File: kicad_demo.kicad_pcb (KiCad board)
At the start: 2 copper layers, 100 x 50 mm, 29 parts, among them P1 pwr, P2 key, Q1 BC546, Q2 BC546, Q3 BC546, Y1 7020 kHz

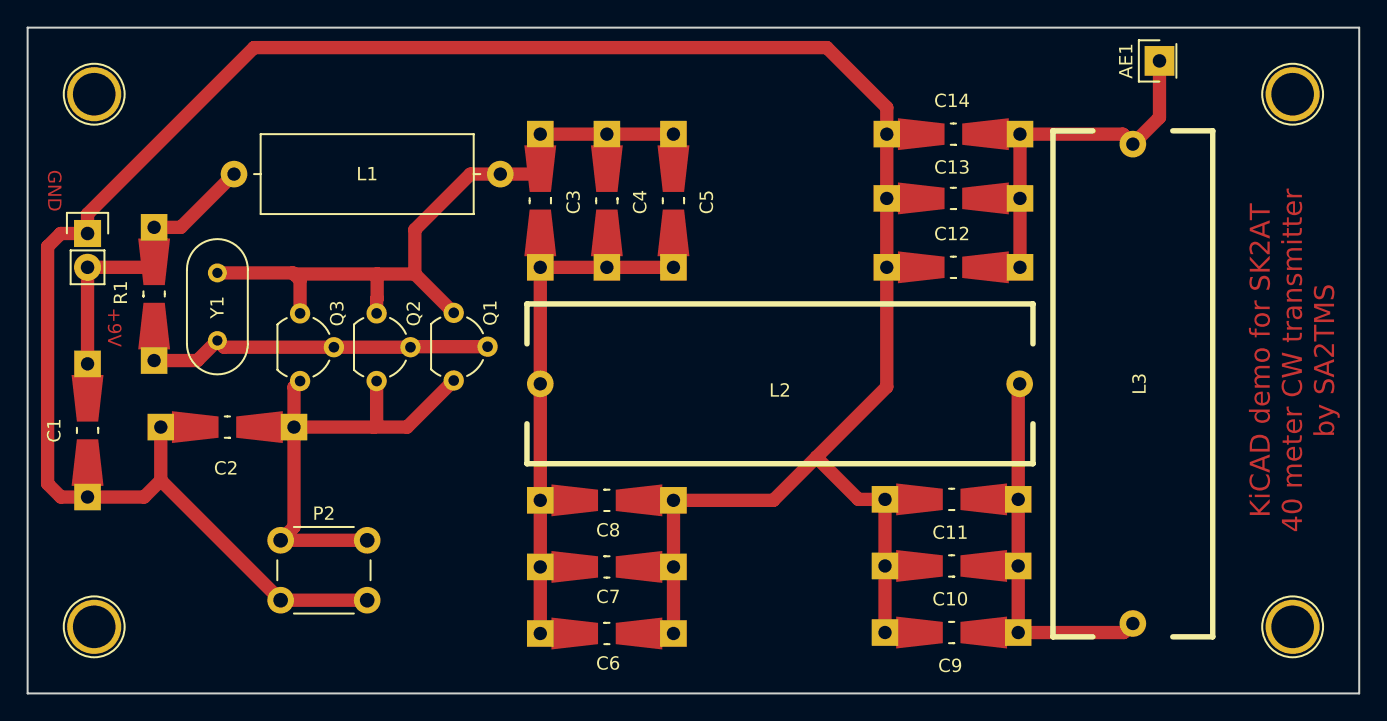
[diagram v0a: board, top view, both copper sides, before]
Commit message: Add test points, winding instruction on F.SilkS
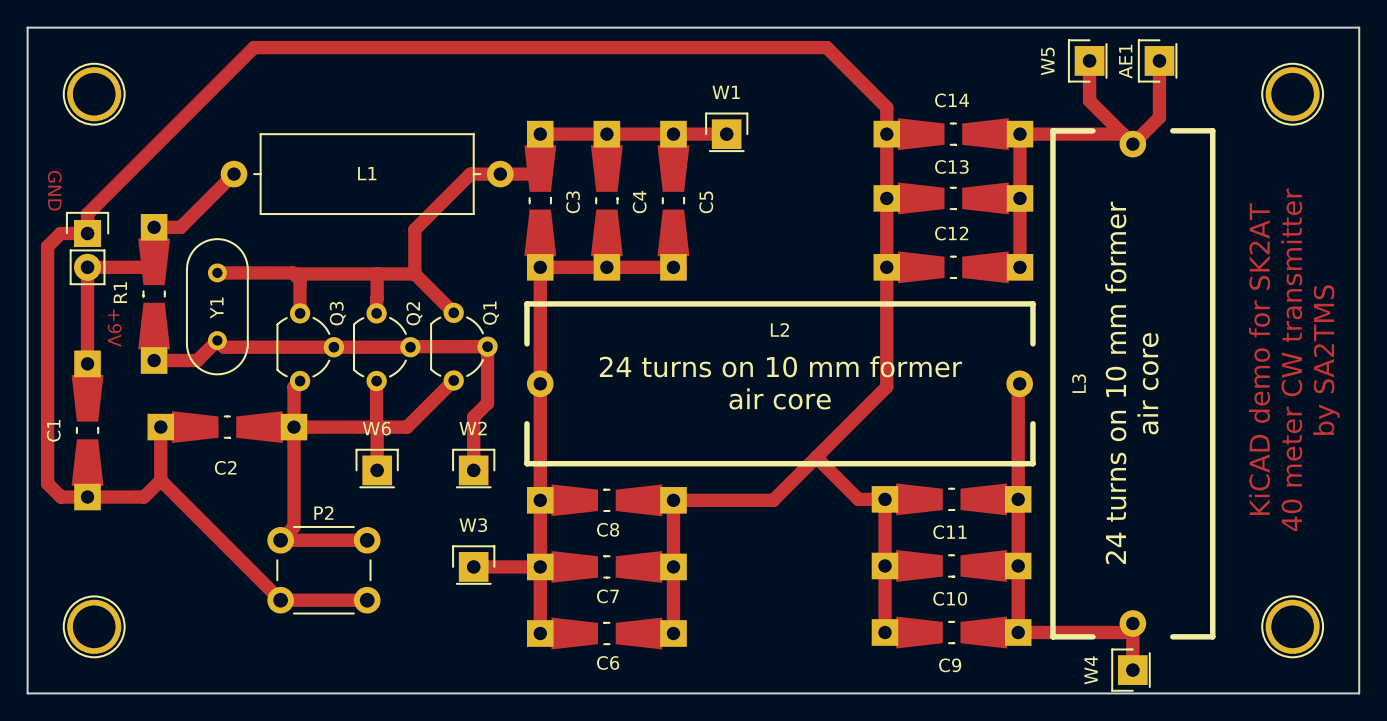
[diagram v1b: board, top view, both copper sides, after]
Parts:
- added W1: TEST_1P, Pin_Headers:Pin_Header_Straight_1x01, F.Cu at (102.5, 83.0)
- added W2: TEST_1P, Pin_Headers:Pin_Header_Straight_1x01, F.Cu at (83.5, 108.2)
- added W3: TEST_1P, Pin_Headers:Pin_Header_Straight_1x01, F.Cu at (83.5, 115.5)
- added W4: TEST_1P, Pin_Headers:Pin_Header_Straight_1x01, F.Cu at (133.0, 123.2)
- added W5: TEST_1P, Pin_Headers:Pin_Header_Straight_1x01, F.Cu at (129.8, 77.5)
- added W6: TEST_1P, Pin_Headers:Pin_Header_Straight_1x01, F.Cu at (76.2, 108.2)
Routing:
- net Net-(Q1-Pad2): track 28.5 -> 38.3 mm
- net Net-(AE1-Pad1): track 33.6 -> 41.2 mm
- net Net-(C3-Pad2): track 53.0 -> 58.0 mm
- net Net-(C3-Pad1): track 57.5 -> 61.5 mm
- net Net-(C10-Pad1): track 35.4 -> 38.9 mm
- net Net-(C2-Pad1): track 38.6 -> 42.1 mm
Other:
- board text added: "24 turns on 10 mm former air core"

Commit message: License under TAPR Open Hardware License Version 1.0
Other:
- board text added: "Licensed under the TAPR Open Hardware License Version 1.0"
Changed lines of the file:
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@@
     (links 82)
     (no_connects 0)
-    (area 49.924999 74.924999 150.075001 125.075001)
+    (area 49.02384 73.95238 150.100001 126.797619)
     (thickness 1.6)
-    (drawings 13)
+    (drawings 14)
     (tracks 126)
     (zones 0)
@@
   )
   (setup
-    (last_trace_width 1)
+    (last_trace_width 0.5)
     (user_trace_width 1)
     (user_trace_width 1.5)
@@
     )
   )
+  (gr_text "Licensed under the TAPR Open Hardware License Version 1.0" (at 103.75 72) (layer Cmts.User)
+    (effects (font (size 1.5 1.5) (thickness 0.3)))
+  )
   (gr_text "24 turns on 10 mm former\nair core" (at 133 101.75 90) (layer F.SilkS)

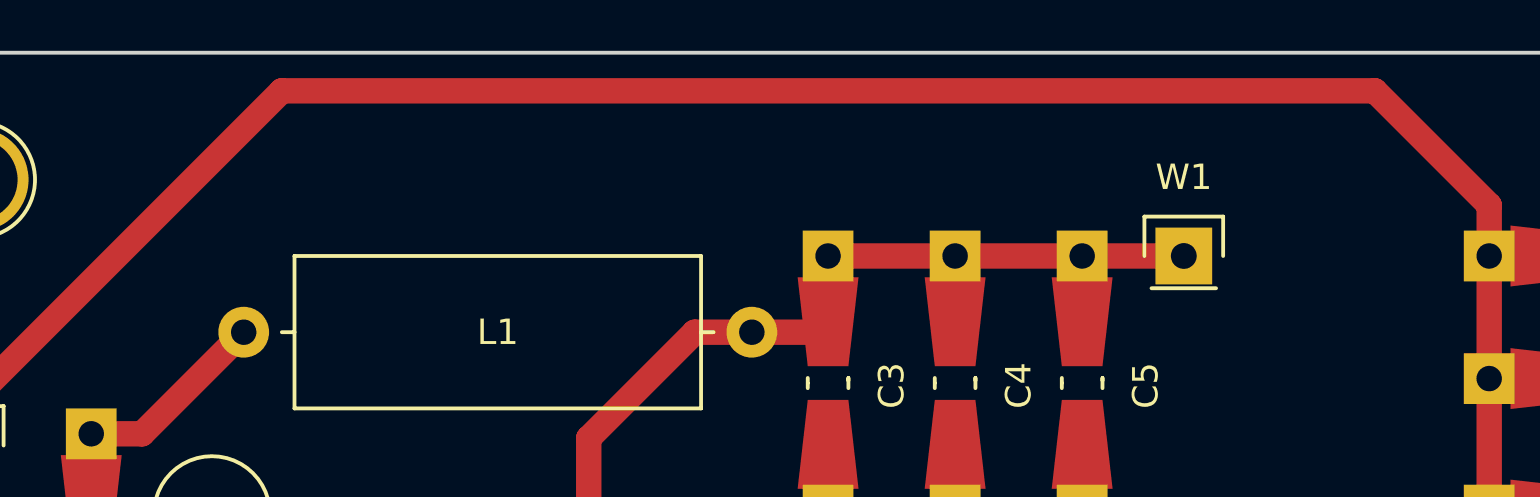
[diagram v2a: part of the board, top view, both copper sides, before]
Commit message: Add some useful power test points
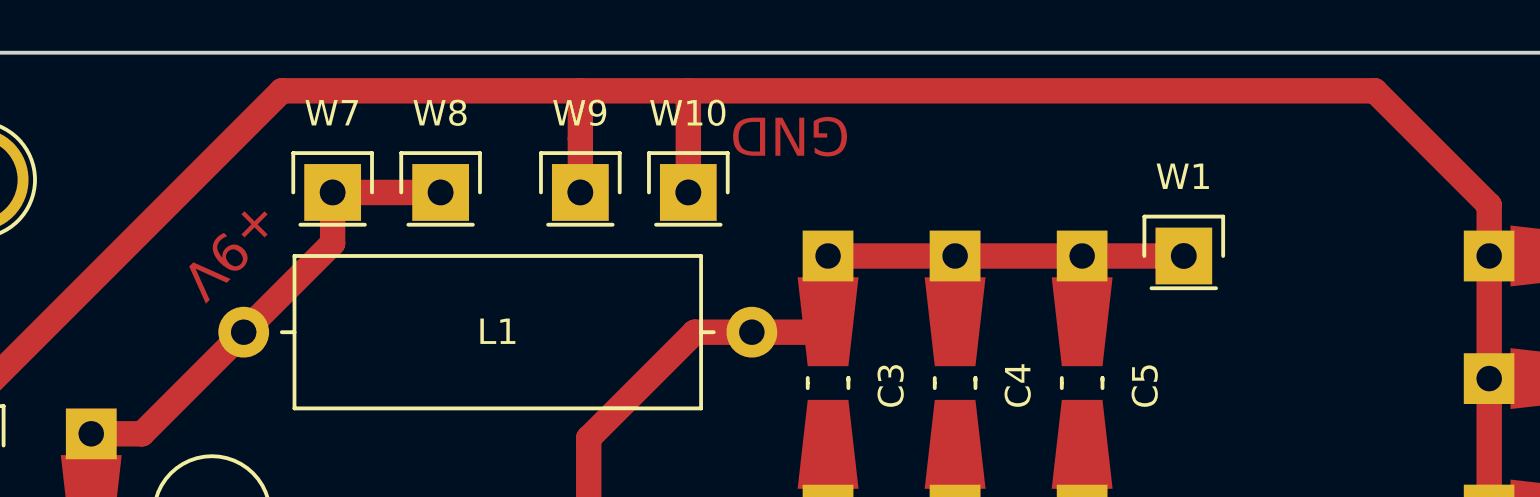
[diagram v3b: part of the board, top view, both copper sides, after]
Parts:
- added W10: TEST_1P, Pin_Headers:Pin_Header_Straight_1x01, F.Cu at (83.0, 80.5)
- added W7: TEST_1P, Pin_Headers:Pin_Header_Straight_1x01, F.Cu at (69.0, 80.5)
- added W8: TEST_1P, Pin_Headers:Pin_Header_Straight_1x01, F.Cu at (73.2, 80.5)
- added W9: TEST_1P, Pin_Headers:Pin_Header_Straight_1x01, F.Cu at (78.8, 80.5)
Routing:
- net +9V: track 25.3 -> 36.5 mm
- net GND: track 217.9 -> 225.9 mm
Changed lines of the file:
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@@
 (kicad_pcb (version 4) (host pcbnew 4.0.5+dfsg1-4)
   (general
-    (links 82)
-    (no_connects 0)
-    (area 49.02384 73.95238 150.100001 126.797619)
+    (links 86)
+    (no_connects 2)
+    (area 49.924999 74.924999 150.075001 125.075001)
     (thickness 1.6)
-    (drawings 14)
-    (tracks 126)
+    (drawings 16)
+    (tracks 134)
     (zones 0)
-    (modules 35)
+    (modules 39)
     (nets 9)
   )
@@
   )
   (setup
-    (last_trace_width 0.5)
+    (last_trace_width 1)
     (user_trace_width 1)
     (user_trace_width 1.5)
@@
     )
   )
+  (module Pin_Headers:Pin_Header_Straight_1x01 (layer F.Cu)
+    (at 69 80.5)
+    (descr "Through hole pin header")
+    (tags "pin header")
+    (fp_text reference W7 (at 0 -3.1) (layer F.SilkS)
+      (effects (font (size 1 1) (thickness 0.15)))
+    )
+    (fp_text value TEST_1P (at 0 -3.1) (layer F.Fab)
+      (effects (font (size 1 1) (thickness 0.15)))
+    )
+    (fp_line (start 1.55 -1.55) (end 1.55 0) (layer F.SilkS) (width 0.15))
+    (fp_line (start -1.75 -1.75) (end -1.75 1.75) (layer F.CrtYd) (width 0.05))
+    (fp_line (start 1.75 -1.75) (end 1.75 1.75) (layer F.CrtYd) (width 0.05))
+    (fp_line (start -1.75 -1.75) (end 1.75 -1.75) (layer F.CrtYd) (width 0.05))
+    (fp_line (start -1.75 1.75) (end 1.75 1.75) (layer F.CrtYd) (width 0.05))
+    (fp_line (start -1.55 0) (end -1.55 -1.55) (layer F.SilkS) (width 0.15))
+    (fp_line (start -1.55 -1.55) (end 1.55 -1.55) (layer F.SilkS) (width 0.15))
+    (fp_line (start -1.27 1.27) (end 1.27 1.27) (layer F.SilkS) (width 0.15))
+    (pad 1 thru_hole rect (at 0 0) (size 2.2352 2.2352) (drill 1.016) (layers *.Cu *.Mask)
+      (net 2 +9V))
+    (model Pin_Headers.3dshapes/Pin_Header_Straight_1x01.wrl
+      (at (xyz 0 0 0))
+      (scale (xyz 1 1 1))
+      (rotate (xyz 0 0 90))
+    )
+  )
+  (module Pin_Headers:Pin_Header_Straight_1x01 (layer F.Cu)
+    (at 73.25 80.5)
+    (descr "Through hole pin header")
+    (tags "pin header")
+    (fp_text reference W8 (at 0 -3.1) (layer F.SilkS)
+      (effects (font (size 1 1) (thickness 0.15)))
+    )
+    (fp_text value TEST_1P (at 0 -3.1) (layer F.Fab)
+      (effects (font (size 1 1) (thickness 0.15)))
+    )
+    (fp_line (start 1.55 -1.55) (end 1.55 0) (layer F.SilkS) (width 0.15))
+    (fp_line (start -1.75 -1.75) (end -1.75 1.75) (layer F.CrtYd) (width 0.05))
+    (fp_line (start 1.75 -1.75) (end 1.75 1.75) (layer F.CrtYd) (width 0.05))
+    (fp_line (start -1.75 -1.75) (end 1.75 -1.75) (layer F.CrtYd) (width 0.05))
+    (fp_line (start -1.75 1.75) (end 1.75 1.75) (layer F.CrtYd) (width 0.05))
+    (fp_line (start -1.55 0) (end -1.55 -1.55) (layer F.SilkS) (width 0.15))
+    (fp_line (start -1.55 -1.55) (end 1.55 -1.55) (layer F.SilkS) (width 0.15))
+    (fp_line (start -1.27 1.27) (end 1.27 1.27) (layer F.SilkS) (width 0.15))
+    (pad 1 thru_hole rect (at 0 0) (size 2.2352 2.2352) (drill 1.016) (layers *.Cu *.Mask)
+      (net 2 +9V))
+    (model Pin_Headers.3dshapes/Pin_Header_Straight_1x01.wrl
+      (at (xyz 0 0 0))
+      (scale (xyz 1 1 1))
+      (rotate (xyz 0 0 90))
+    )
+  )
+  (module Pin_Headers:Pin_Header_Straight_1x01 (layer F.Cu)
+    (at 78.75 80.5)
+    (descr "Through hole pin header")
+    (tags "pin header")
+    (fp_text reference W9 (at 0 -3.1) (layer F.SilkS)
+      (effects (font (size 1 1) (thickness 0.15)))
+    )
+    (fp_text value TEST_1P (at 0 -3.1) (layer F.Fab)
+      (effects (font (size 1 1) (thickness 0.15)))
+    )
+    (fp_line (start 1.55 -1.55) (end 1.55 0) (layer F.SilkS) (width 0.15))
+    (fp_line (start -1.75 -1.75) (end -1.75 1.75) (layer F.CrtYd) (width 0.05))
+    (fp_line (start 1.75 -1.75) (end 1.75 1.75) (layer F.CrtYd) (width 0.05))
+    (fp_line (start -1.75 -1.75) (end 1.75 -1.75) (layer F.CrtYd) (width 0.05))
+    (fp_line (start -1.75 1.75) (end 1.75 1.75) (layer F.CrtYd) (width 0.05))
+    (fp_line (start -1.55 0) (end -1.55 -1.55) (layer F.SilkS) (width 0.15))
+    (fp_line (start -1.55 -1.55) (end 1.55 -1.55) (layer F.SilkS) (width 0.15))
+    (fp_line (start -1.27 1.27) (end 1.27 1.27) (layer F.SilkS) (width 0.15))
+    (pad 1 thru_hole rect (at 0 0) (size 2.2352 2.2352) (drill 1.016) (layers *.Cu *.Mask)
+      (net 3 GND))
+    (model Pin_Headers.3dshapes/Pin_Header_Straight_1x01.wrl
+      (at (xyz 0 0 0))
+      (scale (xyz 1 1 1))
+      (rotate (xyz 0 0 90))
+    )
+  )
+  (module Pin_Headers:Pin_Header_Straight_1x01 (layer F.Cu)
+    (at 83 80.5)
+    (descr "Through hole pin header")
+    (tags "pin header")
+    (fp_text reference W10 (at 0 -3.1) (layer F.SilkS)
+      (effects (font (size 1 1) (thickness 0.15)))
+    )
+    (fp_text value TEST_1P (at 0 -3.1) (layer F.Fab)
+      (effects (font (size 1 1) (thickness 0.15)))
+    )
+    (fp_line (start 1.55 -1.55) (end 1.55 0) (layer F.SilkS) (width 0.15))
+    (fp_line (start -1.75 -1.75) (end -1.75 1.75) (layer F.CrtYd) (width 0.05))
+    (fp_line (start 1.75 -1.75) (end 1.75 1.75) (layer F.CrtYd) (width 0.05))
+    (fp_line (start -1.75 -1.75) (end 1.75 -1.75) (layer F.CrtYd) (width 0.05))
+    (fp_line (start -1.75 1.75) (end 1.75 1.75) (layer F.CrtYd) (width 0.05))
+    (fp_line (start -1.55 0) (end -1.55 -1.55) (layer F.SilkS) (width 0.15))
+    (fp_line (start -1.55 -1.55) (end 1.55 -1.55) (layer F.SilkS) (width 0.15))
+    (fp_line (start -1.27 1.27) (end 1.27 1.27) (layer F.SilkS) (width 0.15))
+    (pad 1 thru_hole rect (at 0 0) (size 2.2352 2.2352) (drill 1.016) (layers *.Cu *.Mask)
+      (net 3 GND))
+    (model Pin_Headers.3dshapes/Pin_Header_Straight_1x01.wrl
+      (at (xyz 0 0 0))
+      (scale (xyz 1 1 1))
+      (rotate (xyz 0 0 90))
+    )
+  )
+  (gr_text GND (at 87 78.25 180) (layer F.Cu)
+    (effects (font (size 1.5 1.5) (thickness 0.3)))
+  )
+  (gr_text +9V (at 65 82.75 225) (layer F.Cu)
+    (effects (font (size 1.5 1.5) (thickness 0.3)))
+  )
   (gr_text "Licensed under the TAPR Open Hardware License Version 1.0" (at 103.75 72) (layer Cmts.User)
     (effects (font (size 1.5 1.5) (thickness 0.3)))
@@
   (segment (start 124.523127 87.825832) (end 124.523127 83) (width 1) (layer F.Cu) (net 1))
   (segment (start 124.523127 93) (end 124.523127 87.825832) (width 1) (layer F.Cu) (net 1))
+  (segment (start 73.25 80.5) (end 69 80.5) (width 1) (layer F.Cu) (net 2))
+  (segment (start 69 80.5) (end 69 82.50004) (width 1) (layer F.Cu) (net 2))
+  (segment (start 69 82.50004) (end 65.50004 86) (width 1) (layer F.Cu) (net 2))
   (segment (start 54.5 93) (end 59.087 93) (width 1) (layer F.Cu) (net 2))
   (segment (start 59.087 93) (end 59.5 92.587) (width 1) (layer F.Cu) (net 2))
@@
   (segment (start 61.5013 89.99874) (end 65.50004 86) (width 1) (layer F.Cu) (net 2))
   (segment (start 59.5 92.587) (end 59.5 89.99874) (width 1) (layer F.Cu) (net 2))
+  (segment (start 78.75 76.5) (end 83 76.5) (width 1) (layer F.Cu) (net 3))
+  (segment (start 83 76.5) (end 110.020097 76.5) (width 1) (layer F.Cu) (net 3))
+  (segment (start 83 80.5) (end 83 76.5) (width 1) (layer F.Cu) (net 3))
+  (segment (start 67 76.5) (end 78.75 76.5) (width 1) (layer F.Cu) (net 3))
+  (segment (start 78.75 80.5) (end 78.75 78.3824) (width 1) (layer F.Cu) (net 3))
+  (segment (start 78.75 78.3824) (end 78.75 76.5) (width 1) (layer F.Cu) (net 3))
   (segment (start 54.5 110.25126) (end 52.50051 110.25126) (width 1) (layer F.Cu) (net 3))
   (segment (start 52.50051 110.25126) (end 51.5 109.25075) (width 1) (layer F.Cu) (net 3))
@@
   (segment (start 114.520607 81.00051) (end 114.520607 83) (width 1) (layer F.Cu) (net 3))
   (segment (start 54.5 89) (end 67 76.5) (width 1) (layer F.Cu) (net 3))
-  (segment (start 67 76.5) (end 110.020097 76.5) (width 1) (layer F.Cu) (net 3))
   (segment (start 114.520607 101.979393) (end 109.25 107.25) (width 1) (layer F.Cu) (net 3))
   (segment (start 114.520607 93) (end 114.520607 101.979393) (width 1) (layer F.Cu) (net 3))

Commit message: Final version, hopefully
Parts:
- moved W10 31.7 mm to (114.5, 77.2), turned to 90 degrees
- moved AE1 10.5 mm to (124.5, 77.2)
- moved W5 3.76 mm to (133.5, 77.2)
- moved W9 3.75 mm to (82.5, 80.5)
- moved L2 1.46 mm to (105.8, 100.5)
- moved L3 1.35 mm to (133.5, 100.5)
- moved C12 1.25 mm to (119.5, 91.8)
- moved C13 1.25 mm to (119.5, 86.6)
- moved C14 1.25 mm to (119.5, 81.8)
- moved C3 1.25 mm to (88.5, 86.8)
- moved C4 1.25 mm to (93.5, 86.8)
- moved C5 1.25 mm to (98.5, 86.8)
- moved W1 1.25 mm to (102.5, 81.8)
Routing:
- net Net-(C10-Pad1): track 38.9 -> 52.8 mm
- net GND: track 225.9 -> 222.5 mm
- net Net-(C3-Pad2): track 58.0 -> 59.9 mm
- net Net-(AE1-Pad1): track 41.2 -> 41.8 mm
- net Net-(C3-Pad1): track 61.5 -> 62.1 mm
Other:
- board text added: "40 m CW TX"
- board text removed: "24 turns on 10 mm former air core"
